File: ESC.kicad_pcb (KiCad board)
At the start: 2 copper layers, 50 x 50 mm, 180 parts, among them IC1 MP2456GJ-Z, IC2 AP2112K-3.3TRG1, IC3 DRV8300DPWR, IC4 DRV8300DPWR, IC5 DRV8300DPWR, IC6 DRV8300DPWR, J1 Conn_01x01, J10 Conn_01x01, J11 Conn_01x01, J12 Conn_01x01, J13 SM08B-SRSS-TB_LF__SN_, J14 Conn_01x01, J15 Conn_01x01, J2 Conn_01x01, J3 Conn_01x01, J4 Conn_01x01, J5 Conn_01x01, J6 Conn_01x01, J7 Conn_01x01, J8 Conn_01x01, J9 Conn_01x01, Q1 Q_NMOS, Q10 Q_NMOS, Q11 Q_NMOS, Q12 Q_NMOS, Q13 Q_NMOS, Q14 Q_NMOS, Q15 Q_NMOS, Q16 Q_NMOS, Q17 Q_NMOS, Q18 Q_NMOS, Q19 Q_NMOS, Q2 Q_NMOS, Q20 Q_NMOS, Q21 Q_NMOS, Q22 Q_NMOS, Q23 Q_NMOS, Q24 Q_NMOS, Q3 Q_NMOS, Q4 Q_NMOS, Q5 Q_NMOS, Q6 Q_NMOS, Q7 Q_NMOS, Q8 Q_NMOS, Q9 Q_NMOS, U1 STM32G071KBU6, U2 STM32G071KBU6, U3 STM32G071KBU6, U4 STM32G071KBU6, U7 INA180A1

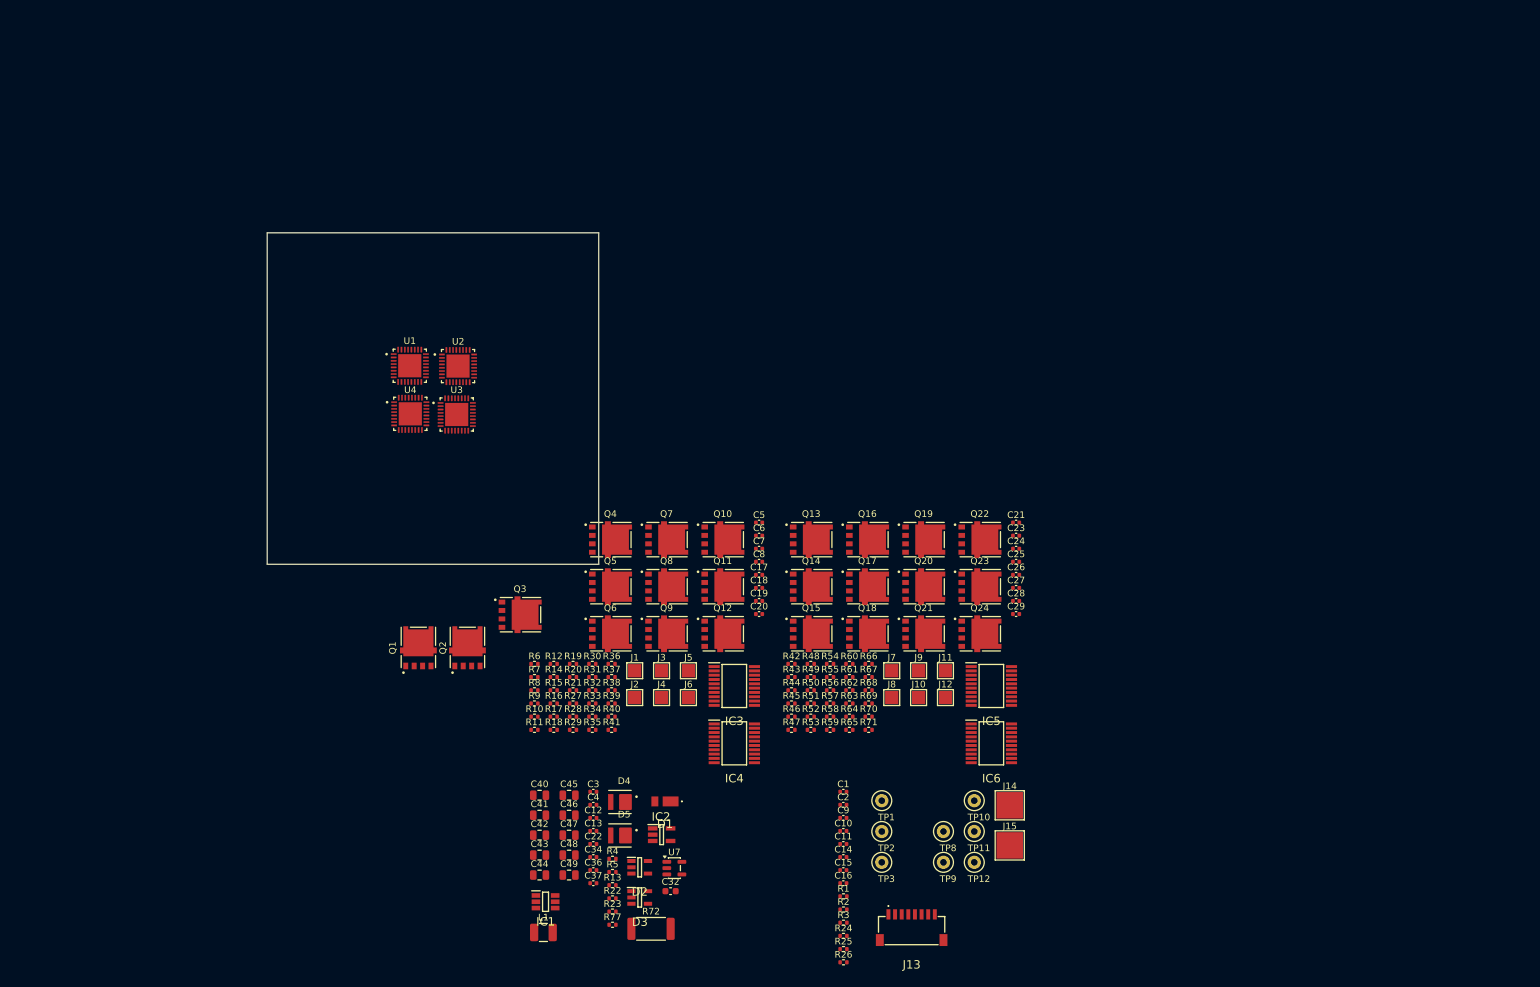
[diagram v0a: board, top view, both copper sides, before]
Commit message: placed first components
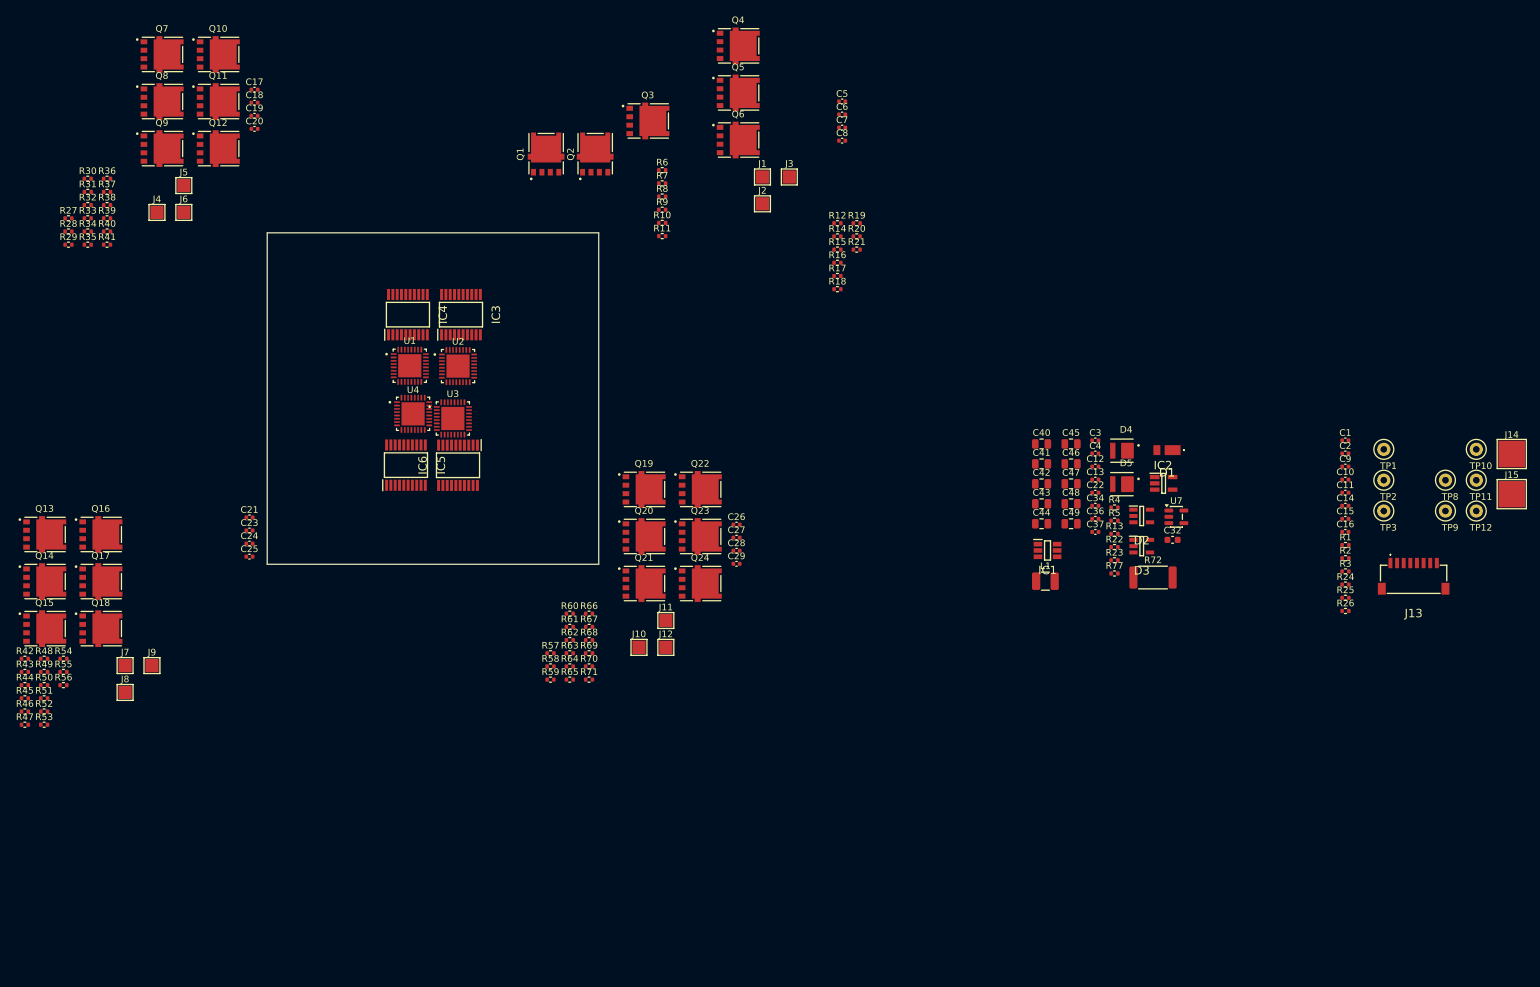
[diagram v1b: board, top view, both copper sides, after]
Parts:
- moved J7 115.6 mm to (-21.4, 65.3)
- moved J8 115.6 mm to (-21.4, 69.3)
- moved J9 115.6 mm to (-17.4, 65.3)
- moved Q13 115.6 mm to (-33.5, 45.5)
- moved Q14 115.6 mm to (-33.5, 52.6)
- moved Q15 115.6 mm to (-33.5, 59.7)
- moved R54 115.6 mm to (-30.7, 64.2)
- moved R55 115.6 mm to (-30.7, 66.2)
- moved R56 115.6 mm to (-30.7, 68.2)
- moved C21 115.6 mm to (-2.68, 42.9)
- moved C23 115.6 mm to (-2.68, 44.9)
- moved C24 115.6 mm to (-2.68, 46.9)
- moved C25 115.6 mm to (-2.68, 48.8)
- moved Q16 115.6 mm to (-25.0, 45.5)
- moved Q17 115.6 mm to (-25.0, 52.6)
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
